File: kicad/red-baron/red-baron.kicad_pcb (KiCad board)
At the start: 2 copper layers, 300 x 300 mm, 10 parts

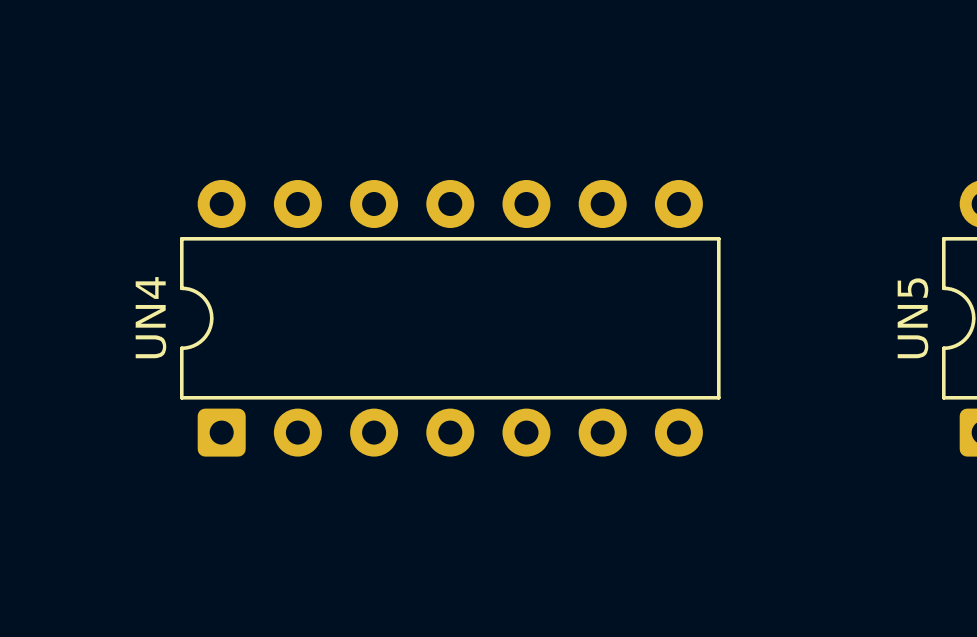
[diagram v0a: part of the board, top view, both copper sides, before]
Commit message: Draw every device at its real package size
The board maps existed to answer "which chip is at C4", and then drew a
24-pin ROM and a 20-pin LS245 as the same 14-pin outline. package_for()
read pin counts from DEVICES, which holds 20 Pong-era parts against the
112 part types the boards actually use, and silently fell back to DIP-14
for the other 92.

tools/packages.py is the pin-count table, kept separate from devices.py
on purpose: packaging needs one number for every part on every board,
while devices.py carries verified pinouts for the parts validate_nets.py
reasons about, and widening that set to satisfy a drawing would let the
extractor trust readings nothing has checked.

688 of 704 devices now size. check_packages.py re-derives 56 of the
entries from KiCAD's symbol library — comparing the highest pin number,
not the pin count, since KiCAD omits no-connects and a 7493 symbol has
ten pins on a DIP-14 — and confirms all 20 parts in DEVICES agree. The
Am2901 slices and the POKEY come from DIP-40 stated on the Battlezone
sheet; the 8316E from the drawing's note that a 2708 may be fitted
instead.

What does not size is now said out loud rather than quietly drawn at 14
pins: four descriptions recorded where the sheet gave no part number,
and the Atari 0351xx ROM/PROM numbers, which get the class default and
are listed as unverified until someone has a board in front of them.

Two things found while reading the corpus for packages, both logged in
asteroids.read.json rather than acted on. The -06 rate multiplier
resolution was recorded and never applied to the board data, and the
parts list disagrees with both readings on designators. F4/H4/J4 take
either an LS670 or an LS170, and the 19-007 pull-up network is fitted
only with the LS170 — same package either way, but a real failure mode.

Also: republishing a board without --machine used to unlink it from its
machine, because most definitions carry no machine of their own and the
link lived only in boards.json. publish_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
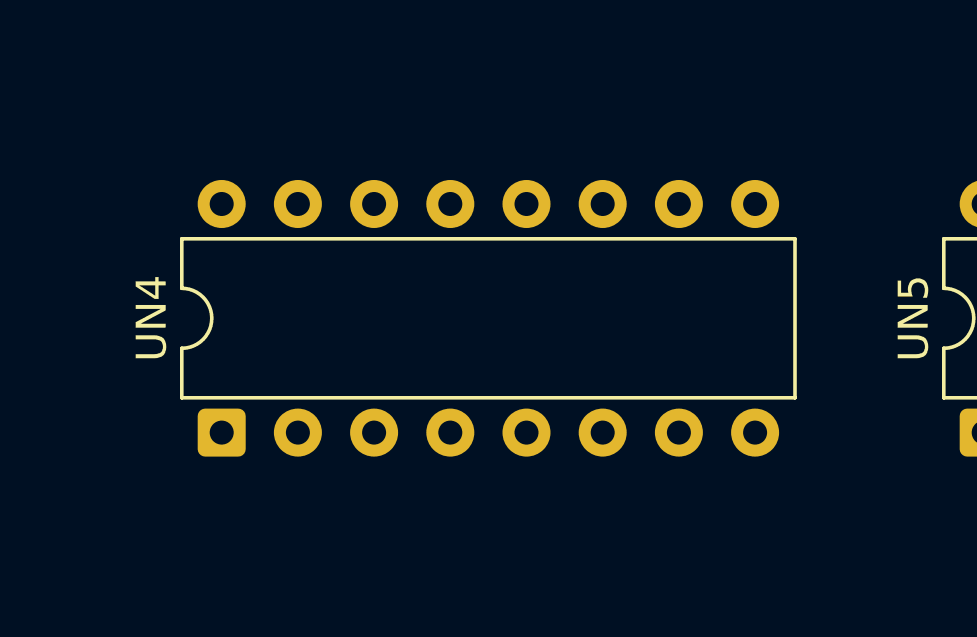
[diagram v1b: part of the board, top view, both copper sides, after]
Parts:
- UN4: footprint DIP-14_W7.62mm -> DIP-16_W7.62mm

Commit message: Drop two grid rows that do not exist, and span the devices that do
Atari's grid alphabet skips G, I, O and Q, and the board definitions
listed G and Q as rows. Every device below F was therefore drawn a row
too low, the rendered board carried two empty bands, and F/H1 looked
like a three-position span for a part 1.2in long on a 0.75in pitch.

Confirmed three ways before touching it. Nothing in any read, signature
or signal record in this repo sits in a G or Q row, while both
neighbours of each are populated on the two densest boards — Battlezone
P:6 R:2, Asteroids-03 P:4 R:3. The sheets' own spanning designators
treat F and H as adjacent and H and J as adjacent, which is only
possible if G and I are not positions. And with G removed, F/H falls out
as an adjacent pair, which is what a 24-pin ROM needs. Pong predates the
convention and legitimately uses G, so it keeps its grid.

Spans are now data rather than prose. A device drawn across two or three
cells is still keyed at its first cell, because that is the only thing
`ics` may be keyed by, but the sheet's own designator goes in a `spans`
map and the footprint is placed at the mean of the cells it names. A
DIP-40 at B/C2 sits between B2 and C2 instead of hanging equally over A2
and C2. The build rejects a span whose rows are not adjacent — that
failure almost always means the grid is wrong, not the span.

Two more inconsistencies found and logged rather than guessed at. Two of
the Math Box's four Am2901 slices carry a span and two do not, though
all four are the same DIP-40 on the same pitch. And asteroids-04.json
carries five devices at the -03 PROM positions alongside the -04 ROMs
and is missing 035144-02 at D/E1, contradicting the substitution table,
memory_by_revision and its own status text in the same breath.

Co-Authored-By: Claude Opus 5 <noreply@anthropic.com>
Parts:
- moved UB6 38.1 mm to (153.0, 246.6)
- moved UN4 19.1 mm to (102.2, 56.1)
- moved UN5 19.1 mm to (127.6, 56.1)
- moved UP5 19.1 mm to (127.6, 37.0)
- moved UP8 19.1 mm to (203.8, 37.0)
- moved UL10 19.0 mm to (254.6, 94.2)
- moved UL5 19.0 mm to (127.6, 94.2)
- moved UM4 19.0 mm to (102.2, 75.2)
- moved UJ4 19.0 mm to (102.2, 132.3)

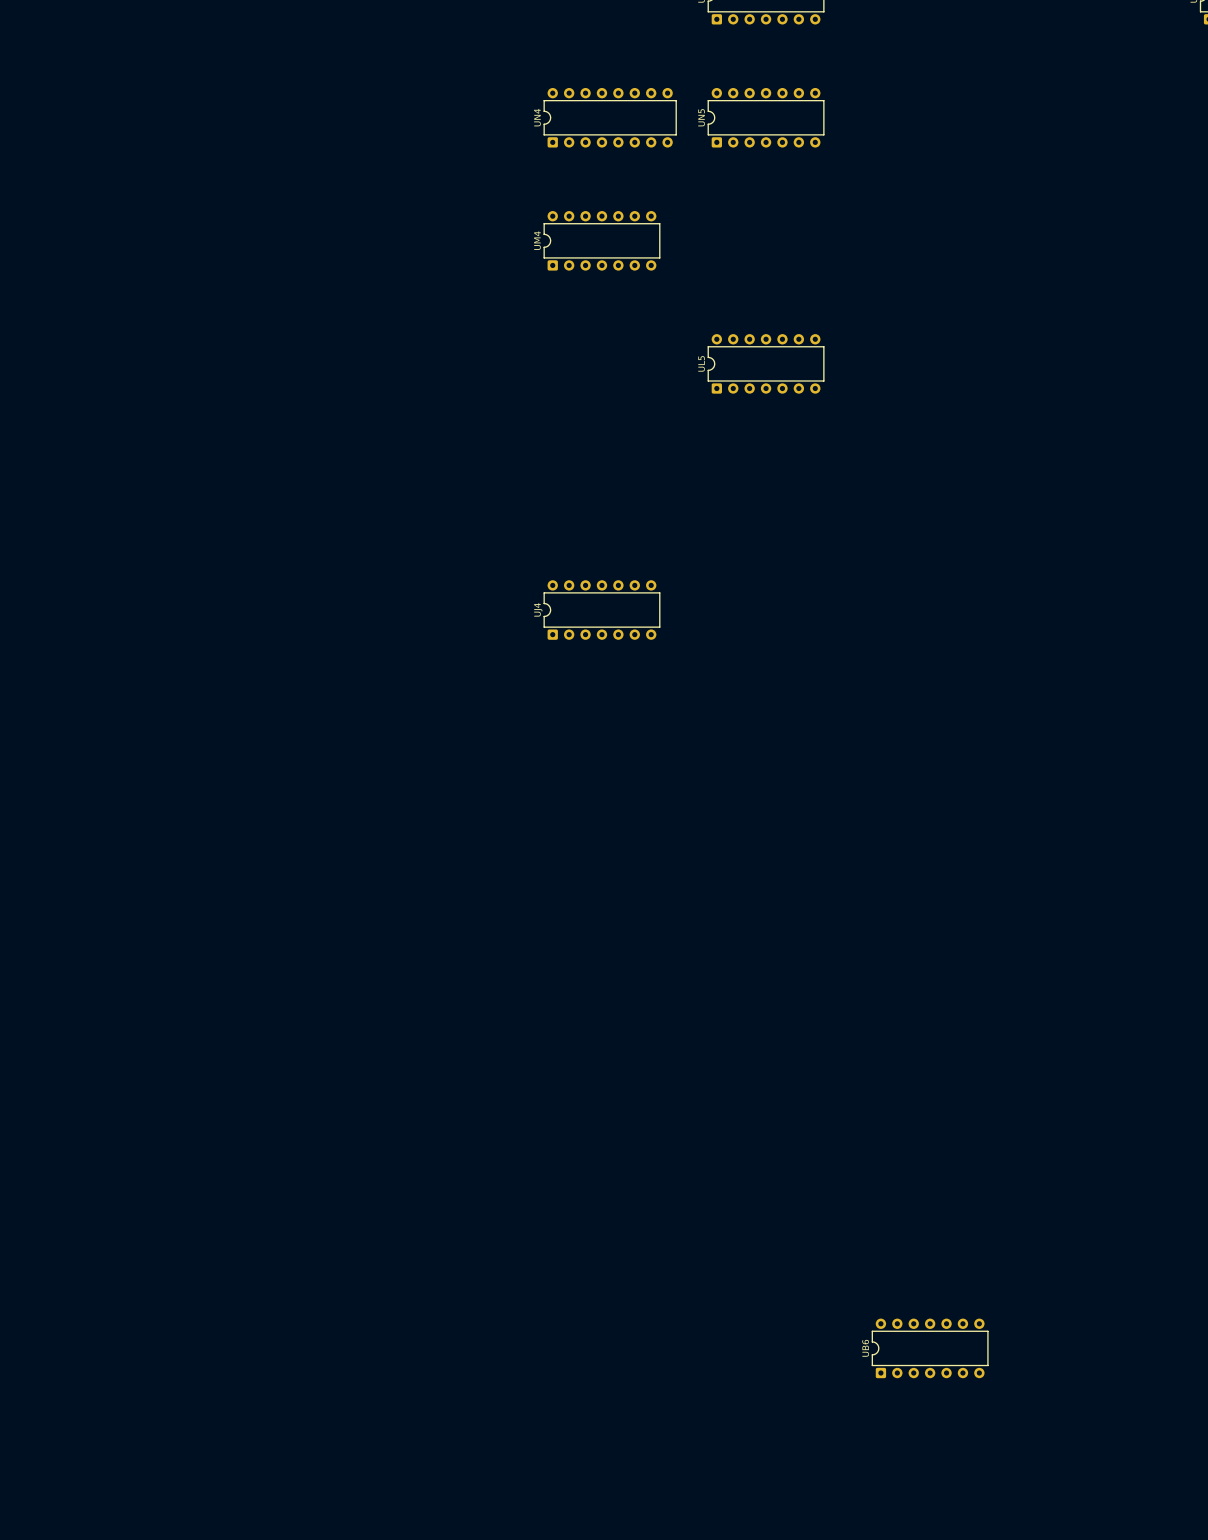
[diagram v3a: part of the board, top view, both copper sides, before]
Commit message: Place the memory devices the IC parts lists cannot reach
Atari stocks ROM, RAM and the microprocessor under its own part numbers
— 90-7033, 036175-01, 90-6013 — not as 37-series IC stock, so the IC
harvest cannot see them however well it reads. That is why Centipede's
ROMs were missing and Red Baron's map had ten devices. merge_memory.py
reads those rows from the same typeset parts lists, under the same rules
as the IC merge: the drawing wins where it exists, two documents must
agree, and nothing is placed whose package cannot be established.

Red Baron 10 to 15, Asteroids Deluxe 92 to 100, Tempest 83 to 88,
Centipede 93 to 95, Missile Command 83 to 85, Lunar Lander 60 to 62.
1,494 devices across the boards, all sized, none contradicted.

Establishing the packages took two corrections, and both were the same
mistake in different clothes.

The first attempt sized Atari stock numbers by correlating a part
against the contact count of the socket at the positions it occupies,
pooled across a machine's documents. That is not a near miss: it put the
2114 at 40 pins, on twelve positions of apparent evidence, because two
printings number the board differently and the correlation was reading
one printing's parts list against another's sockets. Confined to within
a single document it behaves — 33 stock numbers established, 90-6013 by
39 documents agreeing, and 90-7033 correctly refusing to answer rather
than answering wrongly. Those 33 are in packages.py with their
provenance.

The second was the same shape. MAME's dump size was sizing a part from
whatever MAME dumped at that cell, which on Red Baron meant sizing
036175-01 from a dump of 037000-01 — sizing the socket, not the chip.
MAME now sizes a part only when the dump is of that part. Red Baron
loses two devices and keeps thirteen that are right.

Four more parts are sized from MAME's dump sizes alone, where every set
carrying the part agrees and the era leaves no room: 32 bytes and 256
bytes are both bipolar PROMs in a 1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
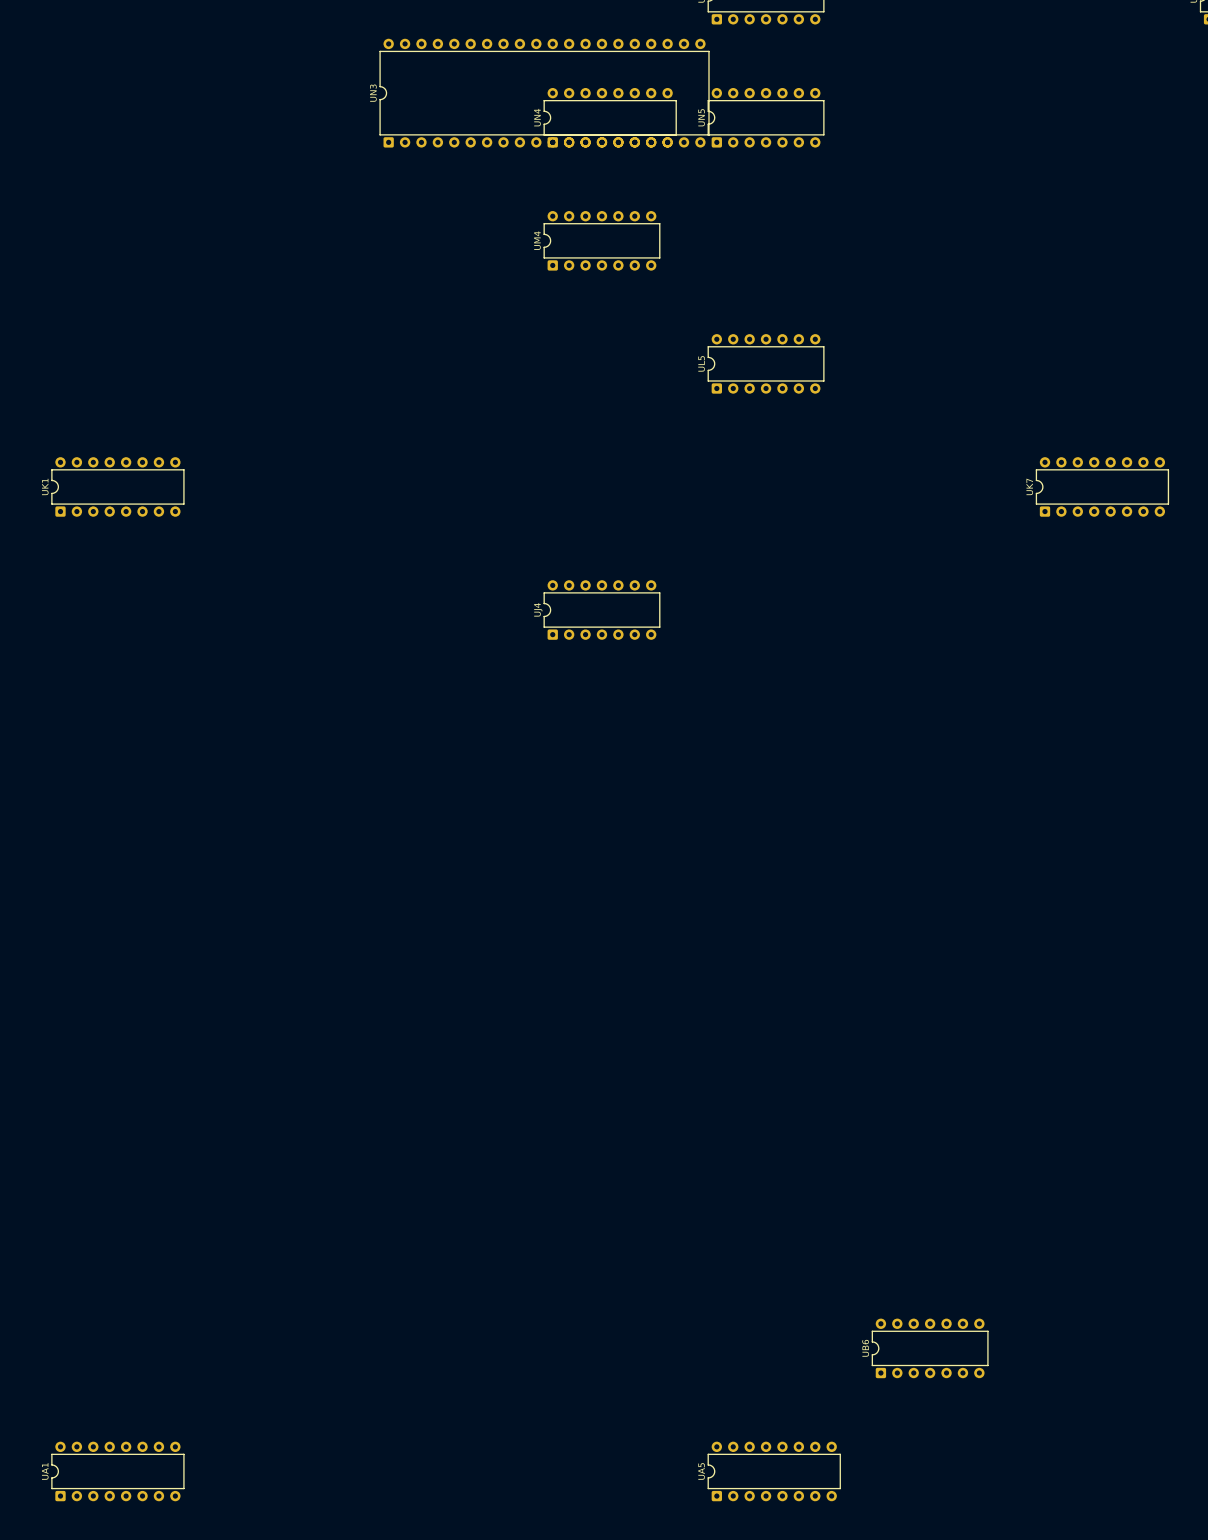
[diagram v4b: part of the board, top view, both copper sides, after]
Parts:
- added UA1: 036174-01, DIP-16_W7.62mm, F.Cu at (26.0, 265.6)
- added UA5: 036464-01, DIP-16_W7.62mm, F.Cu at (127.6, 265.6)
- added UK1: 036179-01, DIP-16_W7.62mm, F.Cu at (26.0, 113.2)
- added UK7: 036408-01, DIP-16_W7.62mm, F.Cu at (178.4, 113.2)
- added UN3: 90-6013, DIP-40_W15.24mm, F.Cu at (76.8, 56.1)

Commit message: Fill four thin boards and add four more, from the parts lists
The parts-list harvest was described as swept. It was swept for finding new
machines to hand-read; it had not been run against the boards already here.
Running it over all 2,389 cached documents finds 29 boards where there was
one, and 1,864 devices where there were 1,365.

Red Baron goes from 15 devices to 66 and Warlords from 12 to 57 — both were
publishing a near-empty map that read as if the machine had nothing to offer.
Gravitar (68), Space Duel (70), Fast Freddie (79) and Red Baron's Auxiliary
PCB (18) are new. Tempest gains 5.

Two results are worth more than the device count:

Red Baron's manual covers two PCBs whose designator grids collide — 8
collisions in TM-169, 6 in TM-171 — and locations() resolves a collision by
last write, so harvesting it whole would have merged two boards into one
wrong map without saying so. Split on the figure heading, both go to zero.
The Analog Vector-Generator half then agrees with Battlezone's hand-read game
PCB on 58 of the 63 positions they share, from sources with nothing in common:
six sides of DP-156 read by eye against OCR of two Red Baron parts lists. That
validates the hand read and the harvest at once. Gravitar and Space Duel check
each other the same way, 54 of 62, from different manuals.

The same split withdraws a claim. Red Baron's Auxiliary PCB is not
Battlezone's Auxiliary Math Box 035678-01: it agrees with it on 2 of 14 shared
designators and carries no Am2901 slices and no 82S129 microcode PROMs at all,
where the Math Box has four and six. A 555 sits where Battlezone has a bit
slice. The old note asserting a shared Math Box — and with it the claim that
Battlezone's signature codes apply to Red Baron — is withdrawn rather than
quietly edited, and what it implicates on the game PCB map is logged.

Everything else was already at its evidence limit: Crash 'n Score, Monte Carlo,
Asteroids Deluxe, Centipede, Football, Missile Command and the nine
single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
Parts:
- added UA6: 74LS194, DIP-16_W7.62mm, F.Cu at (153.0, 265.6)
- added UB4: 74LS42, DIP-16_W7.62mm, F.Cu at (102.2, 246.6)
- added UB5: 74LS194, DIP-16_W7.62mm, F.Cu at (127.6, 246.6)
- added UC5: 74LS194, DIP-16_W7.62mm, F.Cu at (127.6, 227.6)
- added UC6: 74S00, DIP-14_W7.62mm, F.Cu at (153.0, 227.6)
- added UC8: 74LS273, DIP-20_W7.62mm, F.Cu at (203.8, 227.6)
- added UD4: 74LS157, DIP-16_W7.62mm, F.Cu at (102.2, 208.5)
- added UD5: 74LS194, DIP-16_W7.62mm, F.Cu at (127.6, 208.5)
- added UD6: 74LS194, DIP-16_W7.62mm, F.Cu at (153.0, 208.5)
- added UD7: 74LS86, DIP-14_W7.62mm, F.Cu at (178.4, 208.5)
- added UE4: 74LS157, DIP-16_W7.62mm, F.Cu at (102.2, 189.4)
- added UE5: 74LS193, DIP-16_W7.62mm, F.Cu at (127.6, 189.4)
- added UE6: 74LS670, DIP-16_W7.62mm, F.Cu at (153.0, 189.4)
- added UF10: 74LS191, DIP-16_W7.62mm, F.Cu at (254.6, 170.4)
- added UF2: 74LS245, DIP-20_W7.62mm, F.Cu at (51.4, 170.4)
- added UF4: 74LS157, DIP-16_W7.62mm, F.Cu at (102.2, 170.4)
- added UF5: 74LS193, DIP-16_W7.62mm, F.Cu at (127.6, 170.4)
- added UF6: 74LS670, DIP-16_W7.62mm, F.Cu at (153.0, 170.4)
- added UF8: 74LS175, DIP-16_W7.62mm, F.Cu at (203.8, 170.4)
- added UF9: 74LS175, DIP-16_W7.62mm, F.Cu at (229.2, 170.4)
- added UH10: 74LS74, DIP-14_W7.62mm, F.Cu at (254.6, 151.3)
- added UH11: 7404, DIP-14_W7.62mm, F.Cu at (280.0, 151.3)
- added UH4: 74LS157, DIP-16_W7.62mm, F.Cu at (102.2, 151.3)
- added UH5: 74LS193, DIP-16_W7.62mm, F.Cu at (127.6, 151.3)
- added UH6: 74LS670, DIP-16_W7.62mm, F.Cu at (153.0, 151.3)
- added UH8: 74LS399, DIP-16_W7.62mm, F.Cu at (203.8, 151.3)
- added UJ10: 74S74, DIP-14_W7.62mm, F.Cu at (254.6, 132.3)
- added UJ5: 74LS32, DIP-14_W7.62mm, F.Cu at (127.6, 132.3)
- added UJ6: 74LS191, DIP-16_W7.62mm, F.Cu at (153.0, 132.3)
- added UJ7: 74LS42, DIP-16_W7.62mm, F.Cu at (178.4, 132.3)
- added UJ8: 74LS175, DIP-16_W7.62mm, F.Cu at (203.8, 132.3)
- added UK10: 74LS32, DIP-14_W7.62mm, F.Cu at (254.6, 113.2)
- added UK3: 74LS244, DIP-20_W7.62mm, F.Cu at (76.8, 113.2)
- added UK8: 74LS175, DIP-16_W7.62mm, F.Cu at (203.8, 113.2)
- added UK9: 74S02, DIP-14_W7.62mm, F.Cu at (229.2, 113.2)
- added UL8: 74S260, DIP-14_W7.62mm, F.Cu at (203.8, 94.2)
- added UL9: 74S74, DIP-14_W7.62mm, F.Cu at (229.2, 94.2)
- added UM5: 74LS20, DIP-14_W7.62mm, F.Cu at (127.6, 75.2)
- added UM7: 74LS02, DIP-14_W7.62mm, F.Cu at (178.4, 75.2)
- added UM8: 74LS32, DIP-14_W7.62mm, F.Cu at (203.8, 75.2)
- added UM9: 74LS74, DIP-14_W7.62mm, F.Cu at (229.2, 75.2)
- added UN11: 74LS244, DIP-20_W7.62mm, F.Cu at (280.0, 56.1)
- added UN2: 74LS244, DIP-20_W7.62mm, F.Cu at (51.4, 56.1)
- added UN7: 74LS27, DIP-14_W7.62mm, F.Cu at (178.4, 56.1)
- added UN8: 74LS109, DIP-16_W7.62mm, F.Cu at (203.8, 56.1)
- added UN9: 74LS02, DIP-14_W7.62mm, F.Cu at (229.2, 56.1)
- added UP11: 74LS244, DIP-20_W7.62mm, F.Cu at (280.0, 37.0)
- added UP2: 74LS244, DIP-20_W7.62mm, F.Cu at (51.4, 37.0)
- added UR11: 74LS244, DIP-20_W7.62mm, F.Cu at (280.0, 18.0)
- added UR4: 74LS245, DIP-20_W7.62mm, F.Cu at (102.2, 18.0)
- added UR5: 74LS245, DIP-20_W7.62mm, F.Cu at (127.6, 18.0)
